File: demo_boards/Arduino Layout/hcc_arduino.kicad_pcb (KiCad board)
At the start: 2 copper layers, 53.3 x 57.6 mm, 8 parts, among them J1 BATT, J2 USB_B, J3 D2, J4 D7, J5 D8, J6 IOREF, U1 SAMD21_MOD

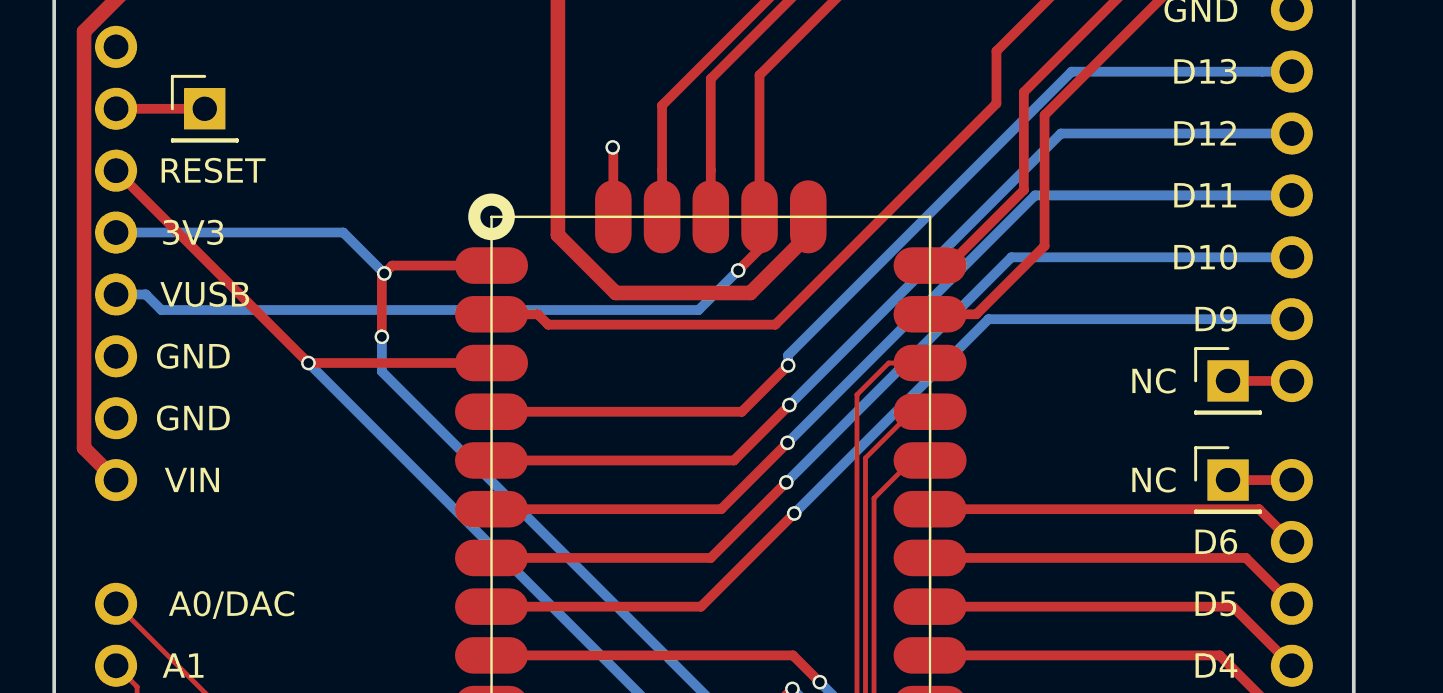
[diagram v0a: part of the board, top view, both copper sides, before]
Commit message: added demo boards
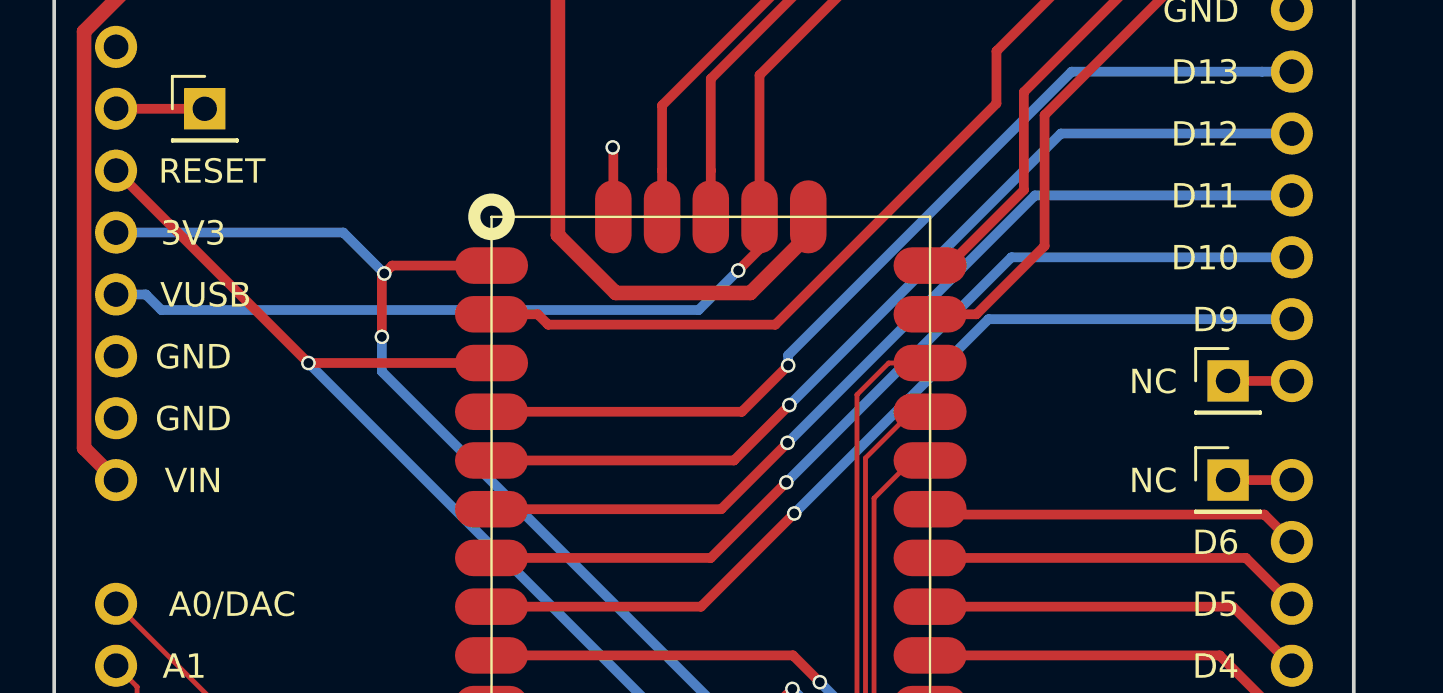
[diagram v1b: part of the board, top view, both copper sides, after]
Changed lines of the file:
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@@
-(kicad_pcb (version 4) (host pcbnew 4.0.7)
+(kicad_pcb (version 4) (host pcbnew 4.0.4-stable)
   (general
     (links 44)
-    (no_connects 4)
-    (area 0 0 0 0)
+    (no_connects 0)
+    (area 61.42 50.05 184.141484 171.150001)
     (thickness 1.6)
-    (drawings 30)
-    (tracks 192)
+    (drawings 32)
+    (tracks 193)
     (zones 0)
     (modules 8)
@@
   )
   (setup
-    (last_trace_width 0.4)
+    (last_trace_width 0.2)
     (user_trace_width 0.2)
     (user_trace_width 0.4)
@@
     (mod_text_size 1 1)
     (mod_text_width 0.15)
-    (pad_size 1.7 1.7)
-    (pad_drill 1)
+    (pad_size 1.2 1.9)
+    (pad_drill 0)
     (pad_to_mask_clearance 0)
     (aux_axis_origin 100 100)
@@
     (pad 6 thru_hole oval (at -3.5 0.35) (size 1.2 1.9) (drill oval 0.6 1.3) (layers *.Cu *.Mask))
     (pad 6 thru_hole oval (at 3.5 0.35 180) (size 1.2 1.9) (drill oval 0.6 1.3) (layers *.Cu *.Mask))
-    (pad 6 smd rect (at 2.9 0.35 180) (size 1.2 1.9) (layers F.Cu F.Mask))
-    (pad 6 smd rect (at -2.9 0.35 180) (size 1.2 1.9) (layers F.Cu F.Mask))
+    (pad 6 smd rect (at 2.9 0.35 180) (size 1.2 1.9) (layers F.Cu F.Paste F.Mask))
+    (pad 6 smd rect (at -2.9 0.35 180) (size 1.2 1.9) (layers F.Cu F.Paste F.Mask))
     (model ${KISYS3DMOD}/Connectors_USB.3dshapes/USB_Micro-B_Molex-105017-0001.wrl
       (at (xyz 0 0 0))
@@
     )
   )
+  (dimension 58.002155 (width 0.3) (layer Cmts.User)
+    (gr_text "58.002 mm" (at 83.242537 127.029935 89.5060831) (layer Cmts.User)
+      (effects (font (size 1.5 1.5) (thickness 0.3)))
+    )
+    (feature1 (pts (xy 120.62 98.35) (xy 82.142587 98.018298)))
+    (feature2 (pts (xy 120.12 156.35) (xy 81.642587 156.018298)))
+    (crossbar (pts (xy 84.342487 156.041573) (xy 84.842487 98.041573)))
+    (arrow1a (pts (xy 84.842487 98.041573) (xy 85.419175 99.17309)))
+    (arrow1b (pts (xy 84.842487 98.041573) (xy 84.246377 99.16298)))
+    (arrow2a (pts (xy 84.342487 156.041573) (xy 84.938597 154.920166)))
+    (arrow2b (pts (xy 84.342487 156.041573) (xy 83.765799 154.910056)))
+  )
+  (dimension 53.502336 (width 0.3) (layer Cmts.User)
+    (gr_text "53.502 mm" (at 132.587769 164.401294 0.5354589856) (layer Cmts.User)
+      (effects (font (size 1.5 1.5) (thickness 0.3)))
+    )
+    (feature1 (pts (xy 159.12 140.85) (xy 159.350386 165.501235)))
+    (feature2 (pts (xy 105.62 141.35) (xy 105.850386 166.001235)))
+    (crossbar (pts (xy 105.825153 163.301353) (xy 159.325153 162.801353)))
+    (arrow1a (pts (xy 159.325153 162.801353) (xy 158.204179 163.398276)))
+    (arrow1b (pts (xy 159.325153 162.801353) (xy 158.193218 162.225485)))
+    (arrow2a (pts (xy 105.825153 163.301353) (xy 106.957088 163.877221)))
+    (arrow2b (pts (xy 105.825153 163.301353) (xy 106.946127 162.70443)))
+  )
   (gr_text RX/D0 (at 154.46 151.14) (layer F.SilkS)
     (effects (font (size 1 1) (thickness 0.25)) (justify right))
@@
     (effects (font (size 1 1) (thickness 0.25)))
   )
-  (gr_text 3V3 (at 111.534 123.2 360) (layer F.SilkS)
+  (gr_text 3V3 (at 111.534 123.2) (layer F.SilkS)
     (effects (font (size 1 1) (thickness 0.25)))
   )
-  (gr_text RESET (at 112.296 120.66 360) (layer F.SilkS)
+  (gr_text RESET (at 112.296 120.66) (layer F.SilkS)
     (effects (font (size 1 1) (thickness 0.25)))
   )
@@
   (segment (start 135.118589 152.913401) (end 134.623599 152.913401) (width 0.2) (layer F.Cu) (net 20))
   (segment (start 135.368591 152.663399) (end 135.118589 152.913401) (width 0.2) (layer F.Cu) (net 20))
-  (segment (start 141.77 134.525) (end 155.275 134.525) (width 0.4) (layer F.Cu) (net 21))
-  (segment (start 155.275 134.525) (end 156.62 135.87) (width 0.4) (layer F.Cu) (net 21))
+  (segment (start 141.77 134.525) (end 141.990017 134.745017) (width 0.4) (layer F.Cu) (net 21))
+  (segment (start 141.990017 134.745017) (end 155.495017 134.745017) (width 0.4) (layer F.Cu) (net 21))
+  (segment (start 155.495017 134.745017) (end 156.62 135.87) (width 0.4) (layer F.Cu) (net 21))
   (segment (start 154.845 109.975) (end 155.591 109.975) (width 0.4) (layer F.Cu) (net 22))
   (segment (start 155.591 109.975) (end 156.62 108.946) (width 0.4) (layer F.Cu) (net 22))

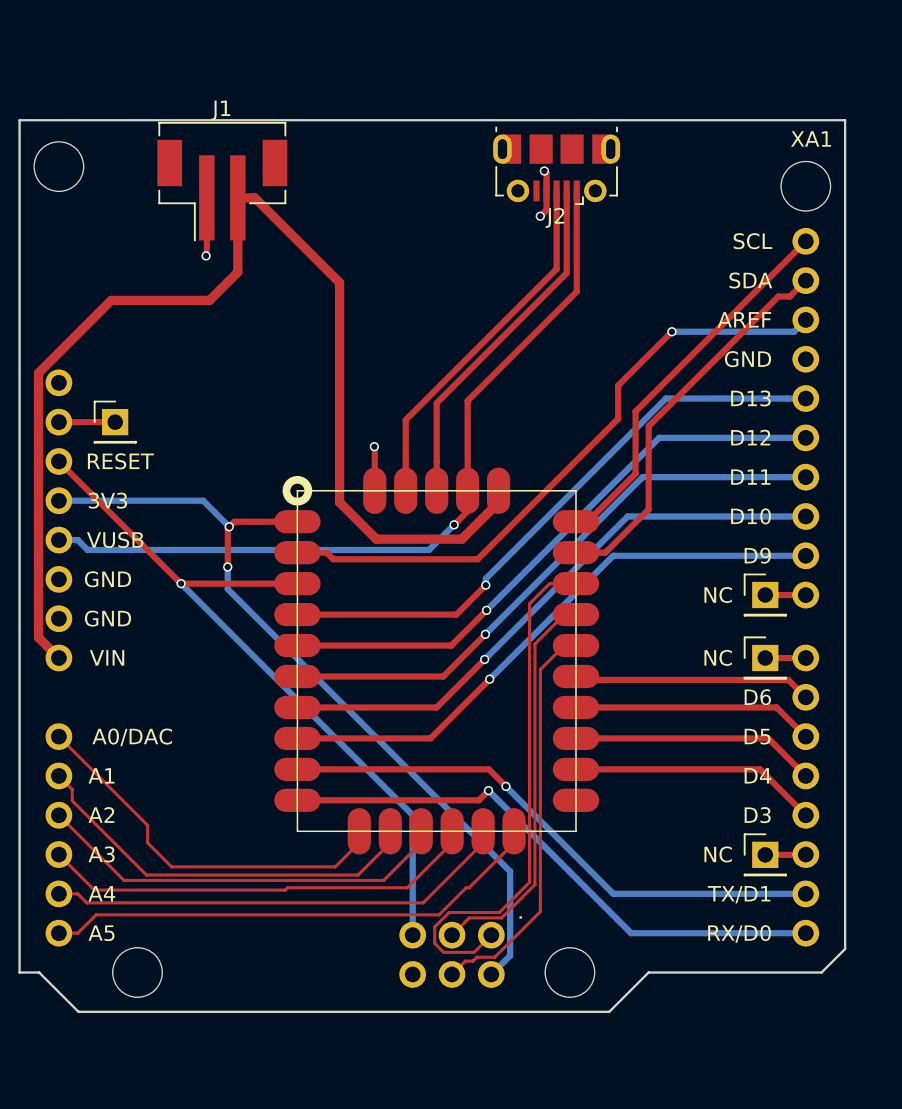
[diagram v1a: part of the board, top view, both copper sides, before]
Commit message: fixed hcc breakout board, added lipo charger
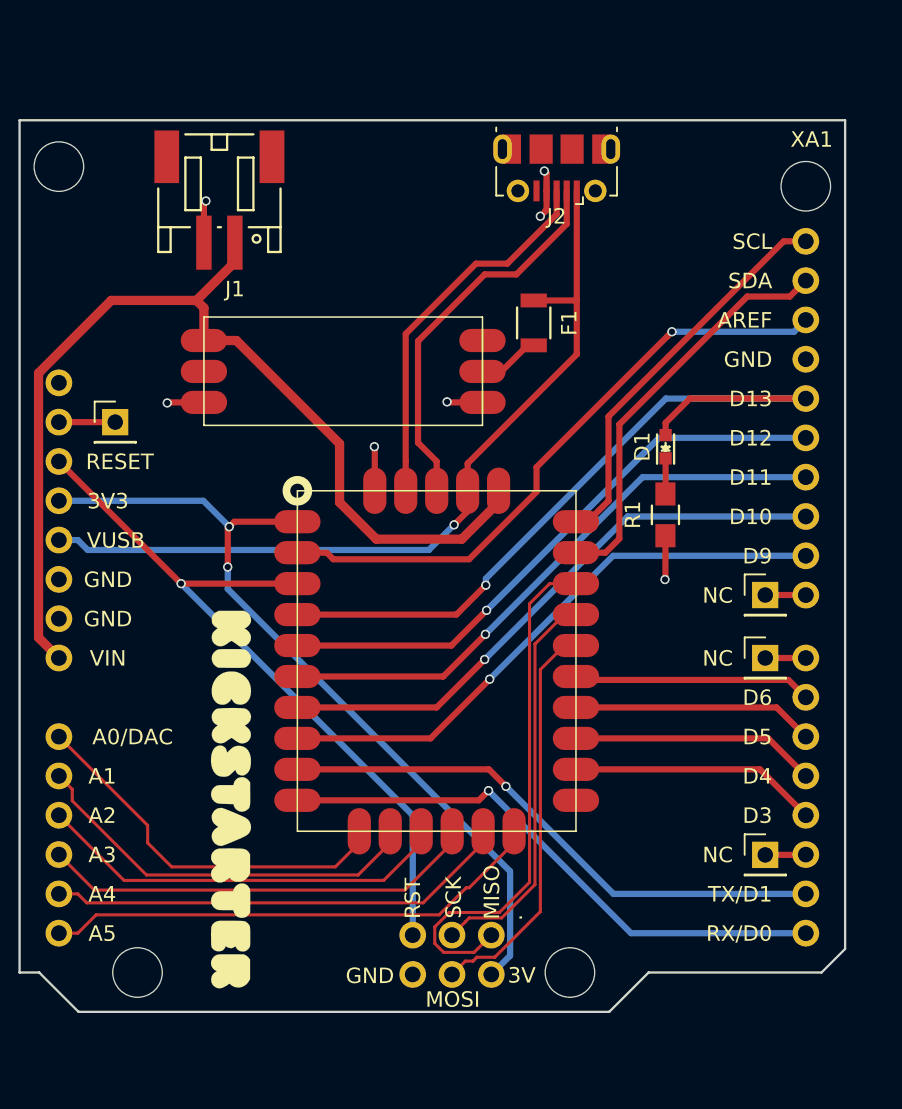
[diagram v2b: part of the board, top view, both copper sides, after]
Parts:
- added D1: LED, LEDs:LED-0603, F.Cu at (147.6, 119.7)
- added F1: Fuse, Resistors_SMD:R_1206, F.Cu at (139.0, 111.7)
- added G***: LOGO, idlehands_libs:KICKSTARTER_LOGO, F.Cu at (119.5, 142.5)
- added G***: LOGO, idlehands_libs:SH_LOGO, F.Cu at (130.3, 103.4)
- added R1: 2k, Resistors_SMD:R_0805_HandSoldering, F.Cu at (147.6, 124.1)
- added U2: charge_mod, idlehands_libs:LIPO_CHARGE_MOD_FOOTPRINT, F.Cu at (126.7, 114.8)
- J1: footprint Connectors_JST:JST_PH_B2B-PH-SM4-TB_02x2.00mm_Straight -> Connectors_JST_PH:Connectors_JST_S2B-PH-SM4-TB
- J2: value USB_B -> USB_OTG
- moved J1 1.26 mm to (118.7, 103.7), turned to 180 degrees
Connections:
- J1 pad 1: GND -> +BATT
- J1 pad 2: +BATT -> GND
- J2 pad 4: GND -> Net-(J2-Pad4)
- J2 pad 5: Net-(J2-Pad5) -> GND
- J2 pad 6: (no net) -> Net-(J2-Pad6)
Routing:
- net D13: track 38.9 -> 49.4 mm
- net +BATT: track 75.4 -> 67.0 mm
- net Net-(F1-Pad2): track 0.00 -> 4.01 mm
- net GND: track 9.78 -> 13.1 mm, vias 4 -> 5
- net Net-(J2-Pad4): track 0.00 -> 3.15 mm, vias 0 -> 2
- net VBUS: track 51.3 -> 54.1 mm
- net Net-(D1-Pad1): track 0.00 -> 2.30 mm
- net Net-(J2-Pad2): track 22.9 -> 25.0 mm
- net Net-(J2-Pad3): track 25.1 -> 26.3 mm
- net SDA: track 25.3 -> 26.5 mm
- net SCL: track 24.7 -> 25.5 mm
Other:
- board text added: "3V"
- board text added: "KICKSTARTER EDITION HCC_MODULE BREAKOUT BOARD IDLEHANDSDEV.com"
- board text added: "MISO"
- board text added: "MOSI"
- board text added: "RST"
- board text added: "SCK"

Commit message: fixed usb connector
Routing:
- net Net-(J2-Pad4): track 3.15 -> 0.00 mm, vias 2 -> 0
- net GND: track 13.1 -> 15.8 mm, vias 5 -> 7
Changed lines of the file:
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@@
     (thickness 1.6)
     (drawings 39)
-    (tracks 219)
+    (tracks 218)
     (zones 0)
     (modules 14)
@@
     (effects (font (size 1 1) (thickness 0.25)))
   )
+  (segment (start 139.22 103.15) (end 139.22 102.13) (width 0.4) (layer F.Cu) (net 1))
+  (segment (start 139.22 102.13) (end 139.1 102.01) (width 0.4) (layer F.Cu) (net 1))
+  (via (at 139.1 102.01) (size 0.6) (drill 0.4) (layers F.Cu B.Cu) (net 1))
+  (segment (start 139.22 103.15) (end 139.22 104.23) (width 0.4) (layer F.Cu) (net 1))
+  (segment (start 139.22 104.23) (end 138.94 104.51) (width 0.4) (layer F.Cu) (net 1))
+  (via (at 138.94 104.51) (size 0.6) (drill 0.4) (layers F.Cu B.Cu) (net 1))
   (segment (start 147.55 125.43) (end 147.55 128.23) (width 0.4) (layer F.Cu) (net 1))
   (segment (start 147.55 128.23) (end 147.52 128.26) (width 0.4) (layer F.Cu) (net 1))
@@
   (segment (start 136.954 114.816) (end 138.64 113.13) (width 0.4) (layer F.Cu) (net 35))
   (segment (start 138.64 113.13) (end 139.04 113.13) (width 0.4) (layer F.Cu) (net 35))
-  (segment (start 139.87 103.15) (end 139.87 102.006) (width 0.4) (layer F.Cu) (net 37))
-  (segment (start 139.87 102.006) (end 139.728 101.864) (width 0.4) (layer F.Cu) (net 37))
-  (via (at 139.728 101.864) (size 0.6) (drill 0.4) (layers F.Cu B.Cu) (net 37))
-  (segment (start 139.766108 104.486806) (end 139.466109 104.786805) (width 0.4) (layer F.Cu) (net 37))
-  (segment (start 139.87 104.382914) (end 139.766108 104.486806) (width 0.4) (layer F.Cu) (net 37))
-  (segment (start 139.87 103.15) (end 139.87 104.382914) (width 0.4) (layer F.Cu) (net 37))
-  (via (at 139.466109 104.786805) (size 0.6) (drill 0.4) (layers F.Cu B.Cu) (net 37))
   (segment (start 147.56 120.4293) (end 147.56 122.72) (width 0.4) (layer F.Cu) (net 38))
   (segment (start 147.56 122.72) (end 147.55 122.73) (width 0.4) (layer F.Cu) (net 38))

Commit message: small changes
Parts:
- added G***: LOGO, project_footprints:qrcode_youtube, B.Cu at (125.7, 137.9)
- U1: footprint idlehands_libs:SAMD_HCC_G_FOOT -> project_footprints:SAMD_HCC_G_FOOT
- U2: footprint idlehands_libs:LIPO_CHARGE_MOD_FOOTPRINT -> project_footprints:LIPO_CHARGE_MOD_FOOTPRINT
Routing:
- net Net-(F1-Pad2): track 4.01 -> 22.2 mm, vias 0 -> 2
- net +BATT: track 67.0 -> 82.8 mm, vias 0 -> 2
